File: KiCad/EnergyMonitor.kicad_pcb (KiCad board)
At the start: 2 copper layers, 99.7 x 49.5 mm, 70 parts, among them J1 Conn_01x04, J10 AudioJack3_Ground_Switch_5_pin, J11 Conn_01x02, J13 Barrel_Jack_Switch, J14 Conn_01x04, J15 Conn_01x04, J16 4P4C, J2 Conn_01x04, J3 Conn_01x04, J4 Conn_01x04, J5 Conn_01x04, J6 Conn_01x04, J7 Conn_01x02, J8 AudioJack3_Ground_Switch_5_pin, J9 AudioJack3_Ground_Switch_5_pin, U1 ESP32_D1_MINI, U2 HT7333

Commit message: circuit design & pcb layout
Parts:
- added R15: 0R, Resistor_SMD:R_0805_2012Metric, B.Cu at (132.7, 97.8)
- added R30: 0R, Resistor_SMD:R_0805_2012Metric, B.Cu at (116.8, 97.8)
- added R31: 0R, Resistor_SMD:R_0805_2012Metric, B.Cu at (103.8, 97.8)
- added R32: 0R, Resistor_SMD:R_0805_2012Metric, B.Cu at (93.7, 102.6)
- added R33: 0R, Resistor_SMD:R_0805_2012Metric, B.Cu at (133.3, 119.7)
- J14: footprint Connector_JST:JST_SH_SM04B-SRSS-TB_1x04-1MP_P1.00mm_Horizontal -> Connector_JST:JST_SH_BM04B-SRSS-TB_1x04-1MP_P1.00mm_Vertical
- moved D5 8.09 mm to (86.0, 84.8), turned to 270 degrees
- moved D4 5.41 mm to (86.0, 89.9), turned to 270 degrees
- moved C10 5.40 mm to (139.4, 104.1), turned to 90 degrees
- moved D2 4.14 mm to (86.0, 100.0), turned to 270 degrees
- moved D3 3.62 mm to (86.0, 94.9), turned to 270 degrees
- moved R28 2.48 mm to (141.3, 108.3)
- moved R29 2.48 mm to (139.4, 108.3)
- moved J14 2.42 mm to (62.5, 119.4)
- moved D6 1.91 mm to (106.0, 81.0)
- moved C9 1.59 mm to (136.2, 108.9)
- moved R25 1.59 mm to (136.2, 107.0)
- moved R26 1.59 mm to (136.2, 103.2)
- moved R27 1.59 mm to (136.2, 105.1)
- moved R14 1.59 mm to (109.5, 81.0)
- moved J15 0.95 mm to (87.3, 122.2)
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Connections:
- J10 pad RN: (no net) -> Net-(J10-PadRN)
- J13 pad 2: GNDA -> GND
- J13 pad 3: GNDA -> GND
- J8 pad RN: (no net) -> Net-(J8-PadRN)
- J9 pad RN: (no net) -> Net-(J9-PadRN)
- U1 pad 10: (no net) -> SPI_MISO
- U1 pad 12: (no net) -> SPI_MOSI
- U1 pad 13: (no net) -> Net-(U1-Pad13)
- U1 pad 14: (no net) -> SPI_CS
- U1 pad 15: (no net) -> Net-(U1-Pad15)
- U1 pad 17: (no net) -> Net-(U1-Pad17)
- U1 pad 18: (no net) -> Net-(U1-Pad18)
- U1 pad 19: (no net) -> Net-(U1-Pad19)
- U1 pad 2: (no net) -> Net-(U1-Pad2)
- U1 pad 20: (no net) -> Net-(U1-Pad20)
- U1 pad 21: (no net) -> Net-(U1-Pad21)
- U1 pad 22: (no net) -> Net-(U1-Pad22)
- U1 pad 23: (no net) -> Net-(U1-Pad23)
- U1 pad 24: (no net) -> Net-(U1-Pad24)
- U1 pad 25: (no net) -> Net-(U1-Pad25)
- U1 pad 26: (no net) -> Net-(U1-Pad26)
- U1 pad 27: (no net) -> Net-(U1-Pad27)
- U1 pad 29: (no net) -> Net-(U1-Pad29)
- U1 pad 3: (no net) -> Net-(U1-Pad3)
- U1 pad 30: (no net) -> Net-(U1-Pad30)
- U1 pad 31: (no net) -> Net-(U1-Pad31)
- U1 pad 32: (no net) -> Net-(U1-Pad32)
- U1 pad 33: ADC1_CH4 -> ADC1_CH5
- U1 pad 35: (no net) -> Net-(U1-Pad35)
- U1 pad 37: (no net) -> Net-(U1-Pad37)
- U1 pad 38: (no net) -> Net-(U1-Pad38)
- U1 pad 4: (no net) -> Net-(U1-Pad4)
- U1 pad 40: (no net) -> Net-(U1-Pad40)
- U1 pad 5: (no net) -> Net-(U1-Pad5)
- U1 pad 6: (no net) -> Net-(U1-Pad6)
- U1 pad 7: ADC1_CH7 -> ADC1_CH4
- U1 pad 8: (no net) -> SPI_CLK
- U1 pad 9: ADC1_CH5 -> ADC1_CH7
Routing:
- net +3V3: track 29.4 -> 261.3 mm
- net ADC1_CH4: track 0.00 -> 76.4 mm, vias 0 -> 4
- net ADC1_CH7: track 0.00 -> 72.7 mm, vias 0 -> 2
- net ADC1_CH6: track 0.00 -> 62.4 mm, vias 0 -> 2
- net ADC1_CH5: track 0.00 -> 39.3 mm
- net 9V_AC: track 0.00 -> 37.6 mm
- net Net-(C1-Pad1): track 0.00 -> 11.4 mm, vias 0 -> 3
- net Net-(C2-Pad1): track 0.00 -> 7.92 mm
- net Net-(C10-Pad1): track 0.00 -> 6.88 mm
- net I2C_SCL: track 62.9 -> 57.7 mm
- net Net-(D1-Pad2): track 0.00 -> 4.81 mm
- net Net-(R25-Pad2): track 0.00 -> 4.57 mm
- net Net-(D1-Pad1): track 0.00 -> 3.30 mm
- net Net-(C9-Pad1): track 0.00 -> 1.92 mm
- net I2C_SDA: track 39.8 -> 40.9 mm
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- added copper zone on B.Cu, net GND
- added copper zone on F.Cu, net GND
- added copper zone on B.Cu, net GNDA
- added copper zone on F.Cu, net GNDA
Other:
- board text added: "1"
- board text added: "2"
- board text added: "3"
- board text added: "I C"
- board text added: "https://github.com/kbhse/EnergyMonitor"
- board text added: "v1.0"
- board text removed: "I2C"

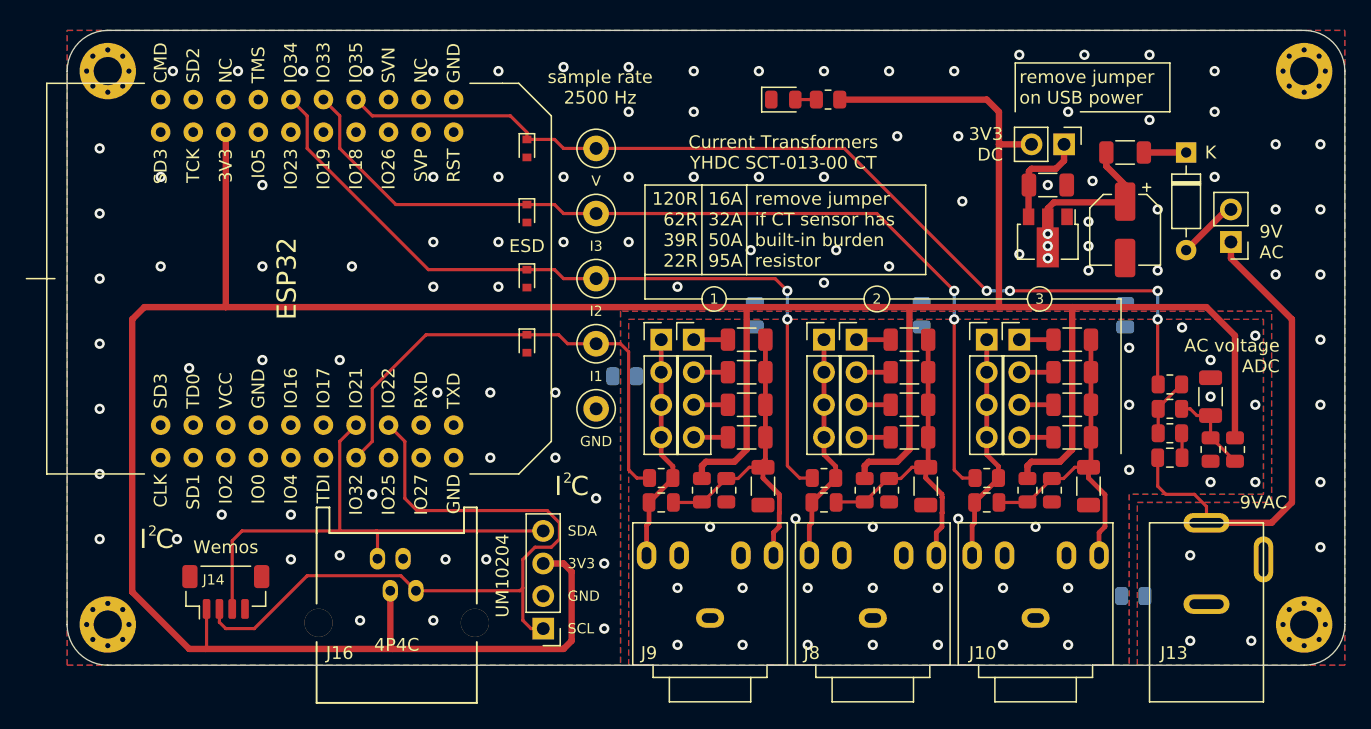
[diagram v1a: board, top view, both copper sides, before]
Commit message: added 2nd I2C port
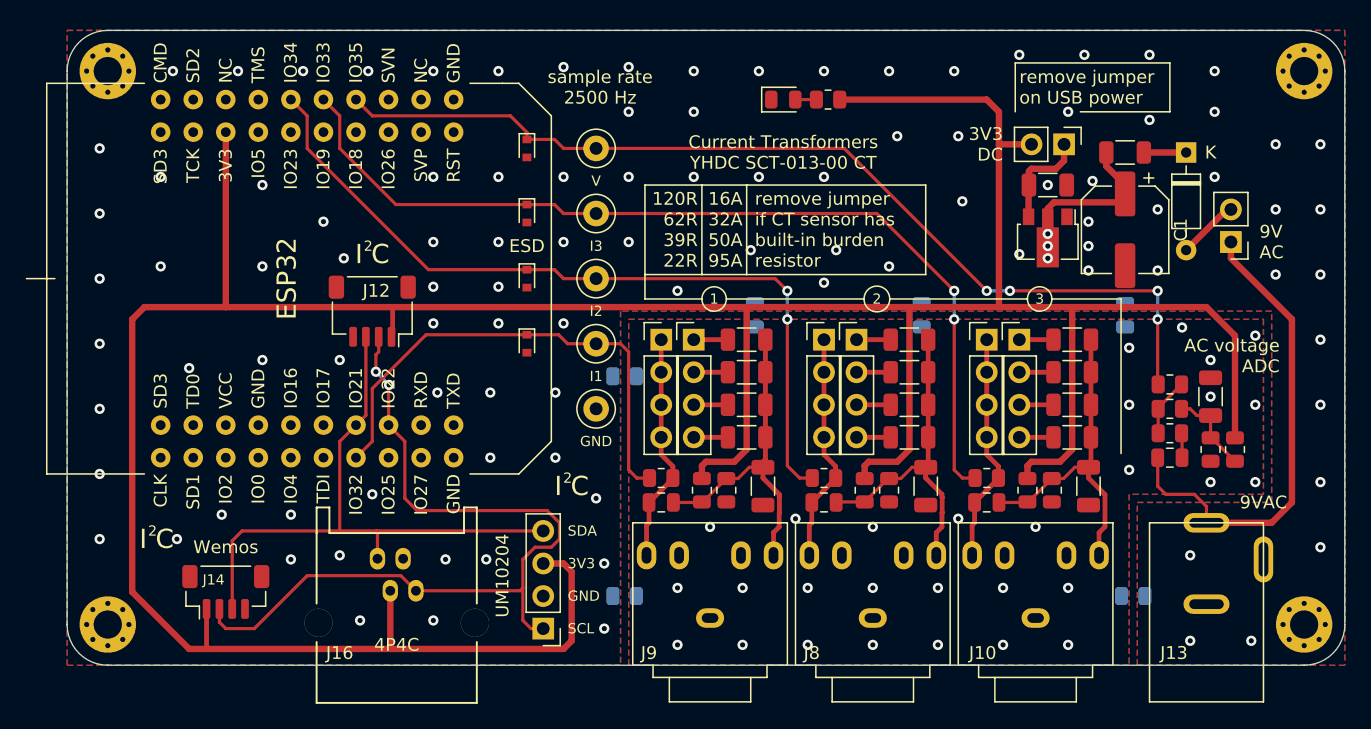
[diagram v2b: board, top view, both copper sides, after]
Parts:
- added J12: Conn_01x04, Connector_JST:JST_SH_SM04B-SRSS-TB_1x04-1MP_P1.00mm_Horizontal, F.Cu at (74.0, 97.5)
- added R34: 0R, Resistor_SMD:R_0805_2012Metric, B.Cu at (93.7, 119.7)
- C1: footprint Capacitor_SMD:CP_Elec_5x4.4 -> Capacitor_SMD:CP_Elec_6.3x5.9
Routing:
- net I2C_SCL: track 57.7 -> 65.1 mm, vias 0 -> 2
- net I2C_SDA: track 40.9 -> 48.1 mm
- net +3V3: track 261.3 -> 263.6 mm
- net GND: vias 98 -> 102

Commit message: added GPIO/SPI port
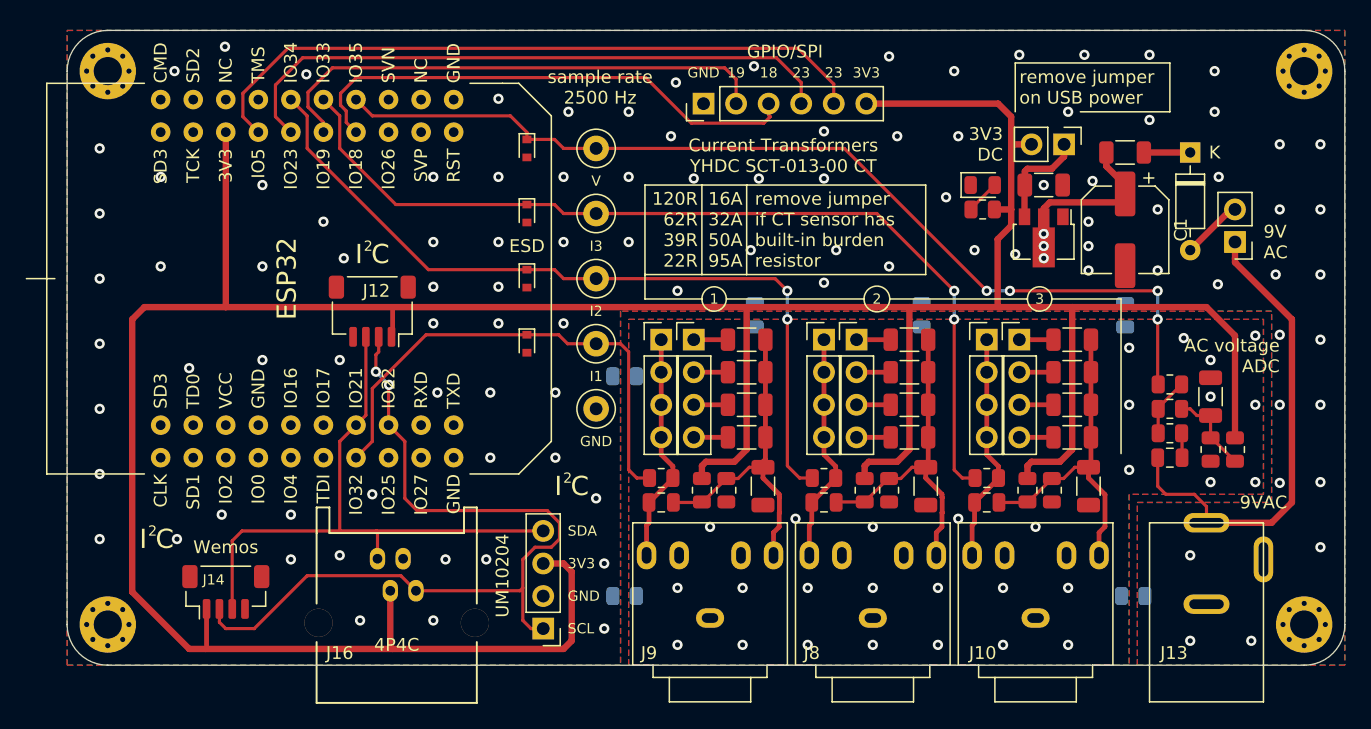
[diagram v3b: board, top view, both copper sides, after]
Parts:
- added J17: Conn_01x06, Connector_PinHeader_2.54mm:PinHeader_1x06_P2.54mm_Vertical, F.Cu at (99.8, 81.3)
- moved D6 16.9 mm to (121.6, 87.6)
- moved R14 14.8 mm to (121.6, 89.5)
- moved C2 0.32 mm to (126.4, 87.6)
- moved U2 0.32 mm to (126.4, 91.8)
- moved D1 0.32 mm to (137.8, 85.1)
- moved J11 0.32 mm to (141.3, 92.1)
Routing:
- net SPI_CS: track 0.00 -> 53.8 mm
- net SPI_MOSI: track 0.00 -> 48.5 mm
- net SPI_CLK: track 0.00 -> 40.3 mm
- net SPI_MISO: track 0.00 -> 40.1 mm
- net Net-(D6-Pad2): track 1.64 -> 2.67 mm
- net +3V3: track 263.6 -> 263.0 mm
- net GND: vias 102 -> 104
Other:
- board text added: "18"
- board text added: "19"
- board text added: "23"
- board text added: "CS"
- board text added: "GPIO/SPI"
- board text added: "MISO"
- board text added: "MOSI"
- board text added: "SCK"
- board text added: "SPI"

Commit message: fabrication gerbers v1.0
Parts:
- added C11: 10uF, Capacitor_SMD:CP_Elec_6.3x5.9, F.Cu at (119.7, 81.9)
- moved D6 3.01 mm to (122.6, 90.5)
- moved R14 3.01 mm to (122.6, 92.4)
- moved D1 1.00 mm to (138.7, 84.8)
- moved J11 1.00 mm to (142.2, 91.8)
- moved C2 1.00 mm to (127.3, 87.3)
- moved J7 1.00 mm to (128.9, 84.1)
- moved U2 1.00 mm to (127.3, 91.4)
- moved R1 1.00 mm to (133.7, 84.8)
- moved C1 1.00 mm to (133.7, 90.8)
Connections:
- J10 pad RN: Net-(J10-PadRN) -> (no net)
- J8 pad RN: Net-(J8-PadRN) -> (no net)
- J9 pad RN: Net-(J9-PadRN) -> (no net)
- U1 pad 13: Net-(U1-Pad13) -> (no net)
- U1 pad 15: Net-(U1-Pad15) -> (no net)
- U1 pad 17: Net-(U1-Pad17) -> (no net)
- U1 pad 18: Net-(U1-Pad18) -> (no net)
- U1 pad 19: Net-(U1-Pad19) -> (no net)
- U1 pad 2: Net-(U1-Pad2) -> (no net)
- U1 pad 20: Net-(U1-Pad20) -> (no net)
- U1 pad 21: Net-(U1-Pad21) -> (no net)
- U1 pad 22: Net-(U1-Pad22) -> (no net)
- U1 pad 23: Net-(U1-Pad23) -> (no net)
- U1 pad 24: Net-(U1-Pad24) -> (no net)
- U1 pad 25: Net-(U1-Pad25) -> (no net)
- U1 pad 26: Net-(U1-Pad26) -> (no net)
- U1 pad 27: Net-(U1-Pad27) -> (no net)
- U1 pad 29: Net-(U1-Pad29) -> (no net)
- U1 pad 3: Net-(U1-Pad3) -> (no net)
- U1 pad 30: Net-(U1-Pad30) -> (no net)
- U1 pad 31: Net-(U1-Pad31) -> (no net)
- U1 pad 32: Net-(U1-Pad32) -> (no net)
- U1 pad 35: Net-(U1-Pad35) -> (no net)
- U1 pad 37: Net-(U1-Pad37) -> (no net)
- U1 pad 38: Net-(U1-Pad38) -> (no net)
- U1 pad 4: Net-(U1-Pad4) -> (no net)
- U1 pad 40: Net-(U1-Pad40) -> (no net)
- U1 pad 5: Net-(U1-Pad5) -> (no net)
- U1 pad 6: Net-(U1-Pad6) -> (no net)
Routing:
- net Net-(C11-Pad1): track 8.05 -> 21.1 mm
- net +3V3: track 263.0 -> 263.8 mm
- net 9V_AC: track 37.4 -> 36.7 mm
- net GND: vias 104 -> 96
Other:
- board text added: "CT1"
- board text added: "CT2"
- board text added: "CT3"
- board text removed: "I1"
- board text removed: "I2"
- board text removed: "I3"
